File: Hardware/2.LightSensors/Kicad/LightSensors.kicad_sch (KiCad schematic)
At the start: 20 parts, among them J1 Conn_01x10_Pin, U1 AS7331, U2 OPT3004

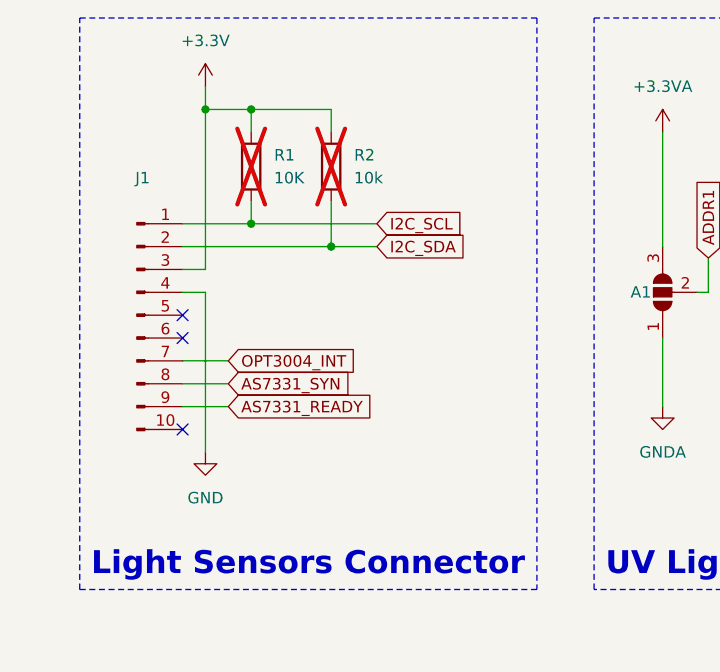
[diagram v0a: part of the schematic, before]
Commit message: Add capacitor bettwen VCC and GND, Update schematic date
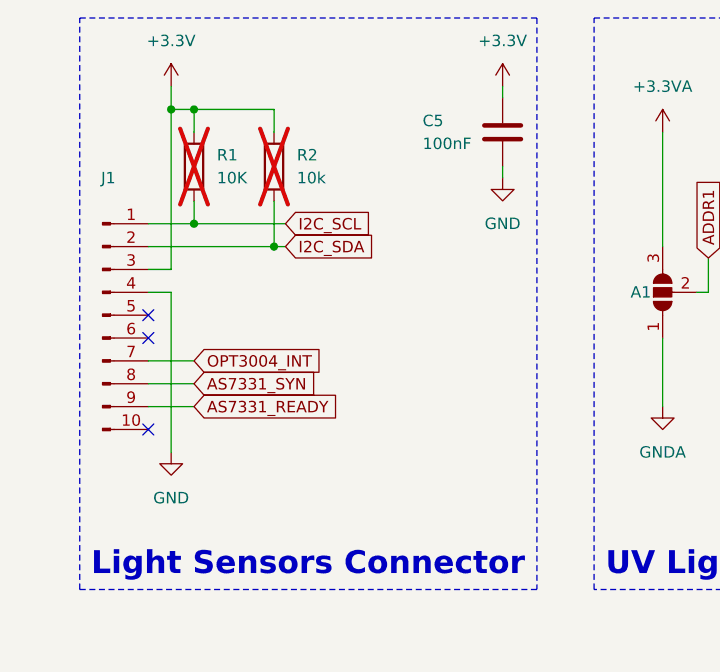
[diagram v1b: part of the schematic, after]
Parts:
- added C5: 100nF, Capacitor_SMD:C_0603_1608Metric, symbol Device:C
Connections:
- net +3.3V: now also C5.1
- net GND: now also C5.2
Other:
- company: (none) -> Github.com/L0R3nz
- moved on the sheet: J1, R1, R2
